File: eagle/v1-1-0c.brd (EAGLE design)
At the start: 313 x 132.9 mm, 176 parts, among them J1 CR22A-44D-2.54DSA(70), J3 26-60-4040, J4 AUDIO_JACK_3.5MM_PTH, J5 DIN5, SW1 3PDT-AQ-SWITCH, SW2 9077-1, U10 7805, U11 74LS10N, U13 74LS04N, U14 4528N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

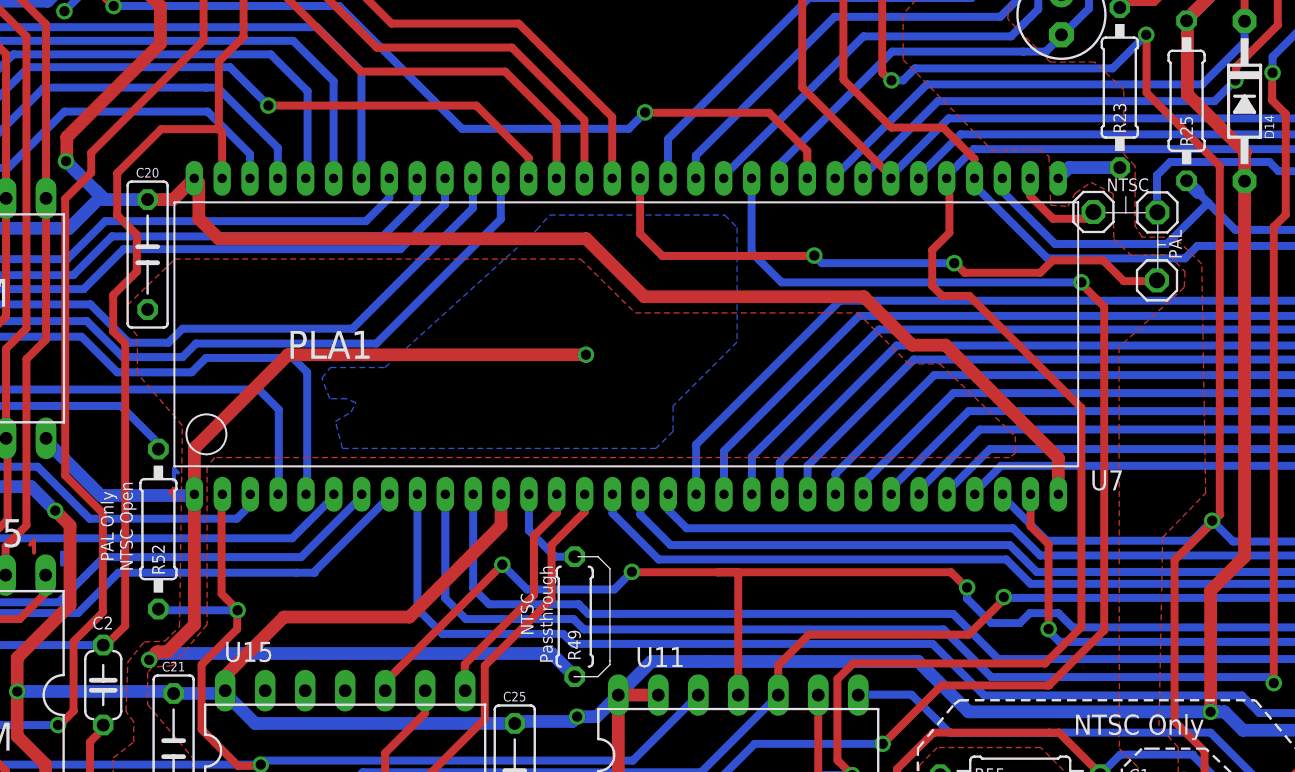
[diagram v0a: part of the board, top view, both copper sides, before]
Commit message: Clean up of values from MW input
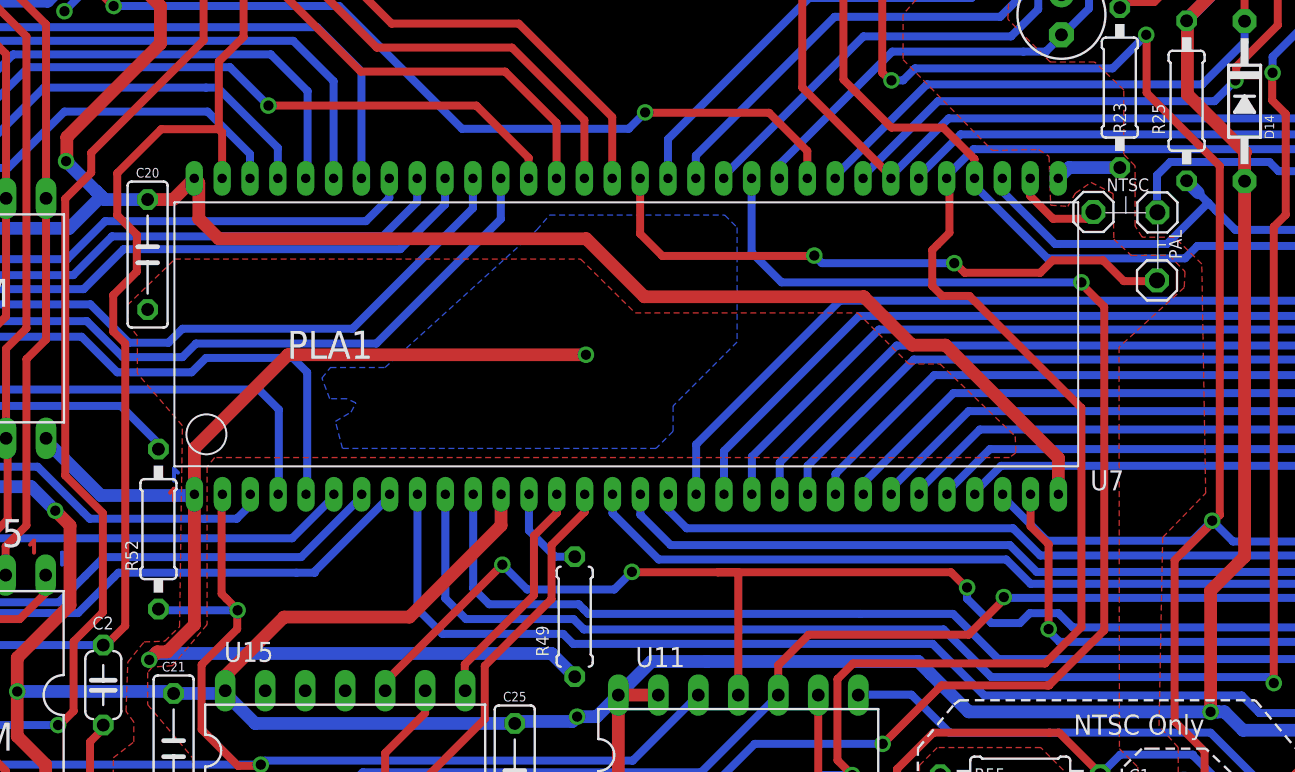
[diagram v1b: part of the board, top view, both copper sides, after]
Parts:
- C16: value 82pF -> 82pF/∞
- C23: value 10pF -> ∞/10pF
- C33: value 680pF -> 680pF/∞
- C34: value 2pF -> 2pF/∞
- C35: value .1uF -> .1uF/∞
- C37: value .001uF -> .001uF/∞
- C39: value 56pF -> 56pF/∞
- C43: value .1uF -> ∞/0.1uF
- R25: value 4.7k -> 4.7k/2.7k
- R49: value 220 -> 0/220
- R50, R51, R52: value 56k -> ∞/56k
- R55: value 47k -> 47k/∞
- R56: value 100k -> 100k/∞
- R57: value 1k -> 1k/∞
- R58: value 10k -> 10k/∞
- R59: value 180 -> 180/∞
- R60: value 470 -> 470/∞
- XTAL2: value 7.15909 Mhz -> ∞/7.15909 Mhz
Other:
- board text removed: "NTSC Passthrough"

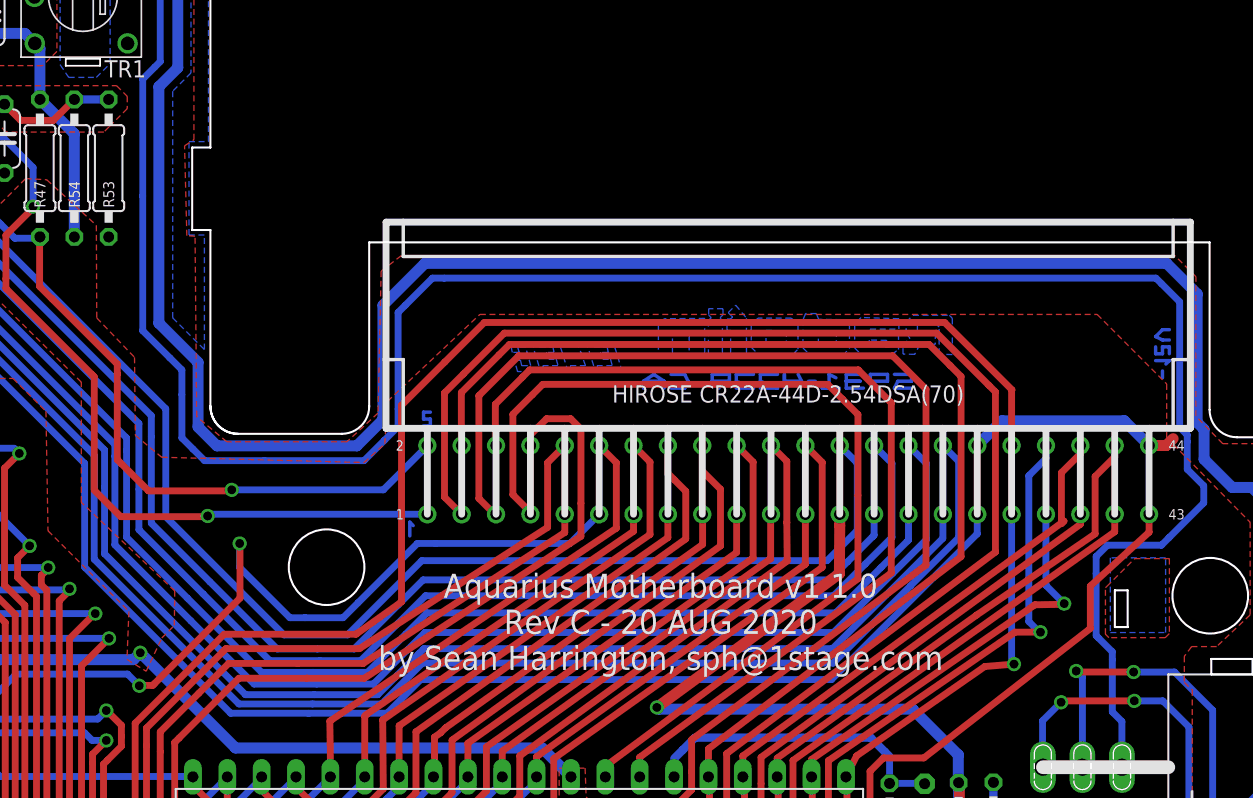
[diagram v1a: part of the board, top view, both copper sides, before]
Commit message: Fix gitignore
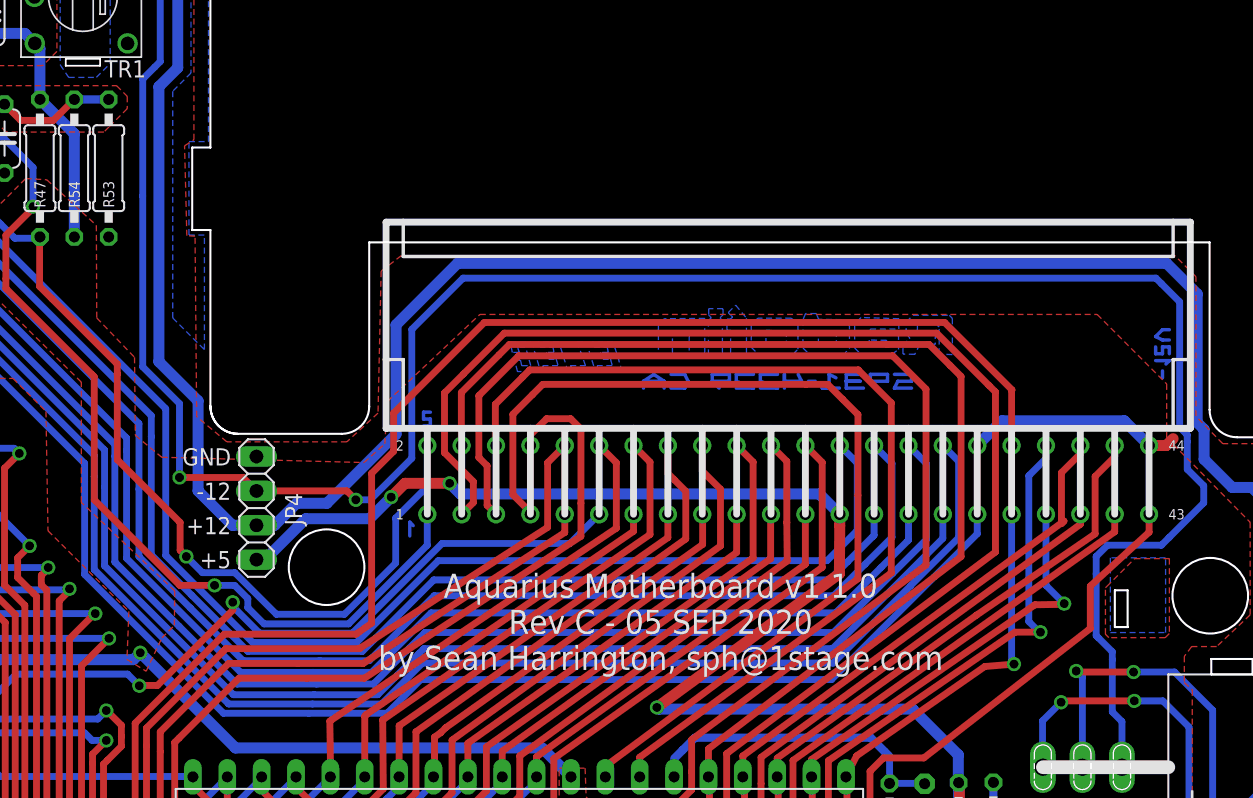
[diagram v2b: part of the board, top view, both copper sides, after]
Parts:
- added JP4: (no value), aquarius2:1X04
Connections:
- net GND: now also JP4.4
- net VCC: now also JP4.1
- net VEE: now also JP4.3
- net VPP: now also JP4.2
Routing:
- net VCC: track 1029.7 -> 1076.1 mm, vias 7 -> 9
- net SND: track 138.8 -> 151.3 mm
- net !CSYNC: track 228.9 -> 237.6 mm
- net VPP: track 503.7 -> 511.1 mm
- net !CE: track 185.5 -> 179.9 mm
- net VEE: track 178.2 -> 183.1 mm, vias 0 -> 2
- net DE00: track 209.8 -> 212.0 mm
- net DE01: track 203.5 -> 205.0 mm
- net DE02: track 208.5 -> 209.7 mm
- net DE03: track 200.0 -> 200.9 mm
- net DE04: track 204.4 -> 205.1 mm
- net !INT: track 123.3 -> 124.0 mm
- net DE05: track 196.8 -> 197.3 mm
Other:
- board text added: "+12"
- board text added: "+5"
- board text added: "-12"
- board text added: "Aquarius Motherboard v1.1.0 Rev C - 05 SEP 2020 by Sean Harrington, sph@1stage.com"
- board text added: "GND"
- board text removed: "Aquarius Motherboard v1.1.0 Rev C - 20 AUG 2020 by Sean Harrington, sph@1stage.com"

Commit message: Updates
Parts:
- J2: device aquarius2:1X16 -> aquarius2:1X17
- moved J2 1.27 mm to (184.4, 27.2)
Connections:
- net GND: now also J2.17
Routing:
- net GND: track 644.3 -> 633.0 mm, vias 22 -> 21
- net !MRST: track 370.4 -> 369.8 mm
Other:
- board text added: "KEY/GND"

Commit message: Updates
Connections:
- net VCC: now also U5.21
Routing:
- net VCC: track 1076.1 -> 1086.0 mm
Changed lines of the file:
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@@
 <wire x1="240.47549375" y1="61.722" x2="237.45289375" y2="58.6994" width="0.8128" layer="16"/>
 <wire x1="236.8296" y1="58.6994" x2="237.45289375" y2="58.6994" width="0.8128" layer="16"/>
+<contactref element="U5" pad="21"/>
+<wire x1="70.3326" y1="9.7536" x2="70.3326" y2="10.3602125" width="0.8128" layer="16"/>
+<wire x1="71.9357875" y1="11.9634" x2="70.3326" y2="10.3602125" width="0.8128" layer="16"/>
+<wire x1="77.9526" y1="9.7536" x2="77.9526" y2="10.0300125" width="0.8128" layer="16"/>
+<wire x1="77.9526" y1="10.0300125" x2="76.0192125" y2="11.9634" width="0.8128" layer="16"/>
+<wire x1="71.9357875" y1="11.9634" x2="74.1172" y2="11.9634" width="0.8128" layer="16"/>
+<wire x1="76.0192125" y1="11.9634" x2="74.1172" y2="11.9634" width="0.8128" layer="16"/>
 </signal>
 <signal name="GND">

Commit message: Errata updates to BRD and SCH and PDFs
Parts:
- added JP5, JP6: (no value), aquarius2:1X01
- R49: device aq-rcl:0207/7 -> aq-rcl:0207/10
- R50, R51: value ∞/56k -> ∞/1.5k
- R52: value ∞/56k -> ∞/100
- moved R49 1.27 mm to (111.5, 21.1)
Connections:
- new net 2Φ-NTSC: JP5.1, U11.12
- net 2Φ: now also JP6.1; no longer U11.12
- net GND: no longer R49.1
- net VCC: now also R49.1
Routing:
- net 2Φ-NTSC: track 0.00 -> 11.5 mm
- net 2Φ: track 122.7 -> 112.7 mm
- net A14: track 262.3 -> 265.7 mm
- net CP/M: track 108.5 -> 111.9 mm
- net VCC: track 1086.0 -> 1086.1 mm, vias 9 -> 8
- net GND: vias 21 -> 22
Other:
- board text added: "Aquarius Motherboard v1.1.0 Rev C - 18 OCT 2020 by Sean Harrington, sph@1stage.com"
- board text added: "Close for NTSC-2Φ"
- board text removed: "Aquarius Motherboard v1.1.0 Rev C - 05 SEP 2020 by Sean Harrington, sph@1stage.com"
